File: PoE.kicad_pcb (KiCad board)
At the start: 2 copper layers, 74 parts, among them J101 ARJM11B1-009-AB-EW2, J102 ARJM11B1-009-AB-EW2, Q201 FDC86244, U101 7490220122, U201 TPS23751PWP, U202 TCMT1107, U203 TCMT1107, U204 TLV431ACDBZR

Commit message: Found footprints
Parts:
- added C2002: 22u, footprints:CAP_WCAP-ASLI_06p3X05p5_WRE, F.Cu at (-95.3, -62.0)
- added C2003: 1u, footprints:CAP_WCAP-ASLI_06p3X05p5_WRE, F.Cu at (-95.3, -53.5)
- added C2005: 47u, footprints:CAP_WCAP-ASLI_06p3X05p5_WRE, F.Cu at (83.3, -22.0)
- added C2006: 47u, footprints:CAP_WCAP-ASLI_06p3X05p5_WRE, F.Cu at (-95.3, -45.1)
- added C2007: 47u, footprints:CAP_WCAP-ASLI_06p3X05p5_WRE, F.Cu at (-95.3, -36.6)
- added C2009: 10u, footprints:CAP_WCAP-ASLI_06p3X05p5_WRE, F.Cu at (-95.3, -28.1)
- added C2011: 1u, Capacitor_SMD:C_0402_1005Metric, F.Cu at (-88.8, -54.7)
- added C2012: 10u, Capacitor_SMD:C_0603_1608Metric, F.Cu at (-88.2, -59.4)
- added D1010: LED, LED_SMD:LED_0402_1005Metric, F.Cu at (50.3, -22.5)
- added FB1001: FerriteBead, Resistor_SMD:R_0805_2012Metric, F.Cu at (-54.0, -71.6)
- added FB1002: FerriteBead, Resistor_SMD:R_0805_2012Metric, F.Cu at (-54.0, -68.7)
- added L2001: 4.7u, Inductor_SMD:L_Abracon_ASPI-4030S, F.Cu at (-87.4, -63.5)
- added R1009: 24.9k, Resistor_SMD:R_0402_1005Metric, F.Cu at (-50.3, -72.1)
- added R1010: 2.2k, Resistor_SMD:R_0402_1005Metric, F.Cu at (-50.3, -70.1)
- added R2011: 0.56, Resistor_SMD:R_0603_1608Metric, F.Cu at (-88.2, -56.9)
- added T2001: ~, footprints:750311320, F.Cu at (58.7, -32.5)
- added TP2001: TestPoint, SparkFun-Connector:TestPoint-1.0mm, F.Cu at (-67.5, -30.0)
- added TP2002: TestPoint, SparkFun-Connector:TestPoint-1.0mm, F.Cu at (-67.5, -27.8)
- added U1002: TCMT1107, footprints:SSOP4_4P40X2P85_VIS, F.Cu at (-50.9, -75.4)
- R2001: renamed from R201; footprint SparkFun-Capacitor:C_0402_1005Metric -> Resistor_SMD:R_0402_1005Metric
- R2006: renamed from R206; value 49.9k -> 49.9
- renumbered C101 to C1001, C102 to C1002, C103 to C1003, C104 to C1004, C105 to C1005, C106 to C1006, C107 to C1007, C108 to C1008, C201 to C2001, C204 to C2004, C208 to C2008, C210 to C2010, C213 to C2013, C214 to C2014, CR201 to CR2001, CR202 to CR2002, CR203 to CR2003, D101 to D1001, D102 to D1002, D103 to D1003, D104 to D1004, D109 to D1005, D105 to D1006, D106 to D1007, D107 to D1008, D108 to D1009, D201 to D2001, D202 to D2002, J102 to J1001, J101 to J1002, Q201 to Q2001, R101 to R1001, R102 to R1002, R103 to R1003, R104 to R1004, R105 to R1005, R106 to R1006, R107 to R1007, R108 to R1008, R202 to R2002, R203 to R2003, R204 to R2004, R205 to R2005, R207 to R2007, R208 to R2008, R209 to R2009, R210 to R2010, R212 to R2012, R213 to R2013, R214 to R2014, R215 to R2015, R216 to R2016, R217 to R2017, R218 to R2018, R219 to R2019, R220 to R2020, TP101 to TP1001, TP102 to TP1002, TP103 to TP1003, TP104 to TP1004, TP105 to TP1005, TP106 to TP1006, TP107 to TP1007, U101 to U1001, U201 to U2001, U202 to U2002, U204 to U2003
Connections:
- C1007 pad 1: Net-(D101-K) -> Net-(D1001-K)
- C1007 pad 2: Net-(D105-A) -> Net-(D1006-A)
- CR2001 pad 2: unconnected-(CR201-Pad2) -> Net-(CR2001-Pad2)
- D1001 pad 1: Net-(D101-K) -> Net-(D1001-K)
- D1002 pad 1: Net-(D101-K) -> Net-(D1001-K)
- D1003 pad 1: Net-(D101-K) -> Net-(D1001-K)
- D1004 pad 1: Net-(D101-K) -> Net-(D1001-K)
- D1006 pad 2: Net-(D105-A) -> Net-(D1006-A)
- D1007 pad 2: Net-(D105-A) -> Net-(D1006-A)
- D1008 pad 2: Net-(D105-A) -> Net-(D1006-A)
- D1009 pad 2: Net-(D105-A) -> Net-(D1006-A)
- R2002 pad 2: unconnected-(R202-Pad2) -> Net-(R2002-Pad2)

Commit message: Updating layout
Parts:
- removed E101, E102: MI1206L501R-10, footprints:FB_MI1206L501R-10
- removed R221: 24.9k, Resistor_SMD:R_0402_1005Metric
- removed R222: 10k, Resistor_SMD:R_0402_1005Metric
- removed U203: TCMT1107, footprints:SSOP4_4P40X2P85_VIS
- C1001, C1002, C1003, C1004, C1005, C1006, C1007, C1008, C2001, C2004, C2008, C2010, C2011, C2012, C2013, C2014, D1001, D1002, D1003, D1004, D1006, D1007, D1008, D1009, D1010, D2001, D2002, R1001, R1002, R1003, R1004, R1005, R1006, R1007, R1008, R1009, R1010, R2001, R2002, R2003, R2004, R2005, R2006, R2007, R2008, R2009, R2010, R2012, R2013, R2014, R2015, R2016, R2017, R2018, R2019, R2020, U1002, U2002, U2003: moved to B.Cu
- moved C2012 218.4 mm to (99.0, 53.0)
- moved C2006 216.5 mm to (106.5, 33.5), turned to 90 degrees
- moved C2011 210.9 mm to (93.5, 51.5), turned to 90 degrees
- moved C2007 205.6 mm to (98.0, 33.5), turned to 90 degrees
- moved L2001 200.3 mm to (76.0, 52.5), turned to 180 degrees
- moved C2003 196.0 mm to (74.5, 44.5), turned to -90 degrees
- moved C2002 190.3 mm to (69.0, 34.0), turned to 90 degrees
- moved R2011 188.8 mm to (63.5, 55.5), turned to 180 degrees
- moved TP1001 182.9 mm to (117.5, 25.0)
- moved U1002 182.6 mm to (78.0, 54.0)
- moved R1010 182.2 mm to (83.0, 54.0), turned to 180 degrees
- moved R2015 179.7 mm to (101.0, 52.4), turned to -90 degrees
- moved TP2002 179.4 mm to (104.0, 25.0)
- moved TP1006 178.6 mm to (116.0, 25.0)
- moved R2019 178.3 mm to (101.0, 54.5), turned to -90 degrees
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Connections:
- D1006 pad 1: unconnected-(D1006-K-Pad1) -> /A_IN
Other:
- board outline added: 102.5 x 33.5 mm
- copper layers 2 -> 4

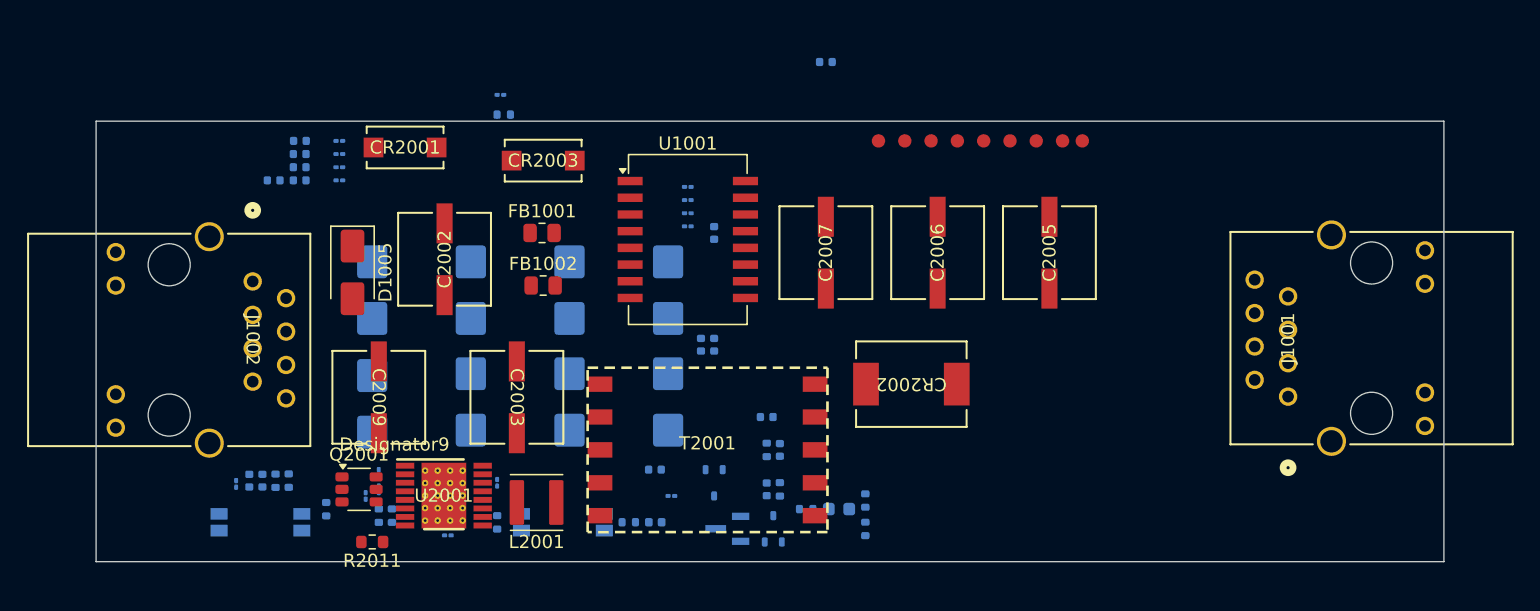
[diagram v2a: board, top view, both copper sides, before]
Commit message: Changed all passive footprints to 0805
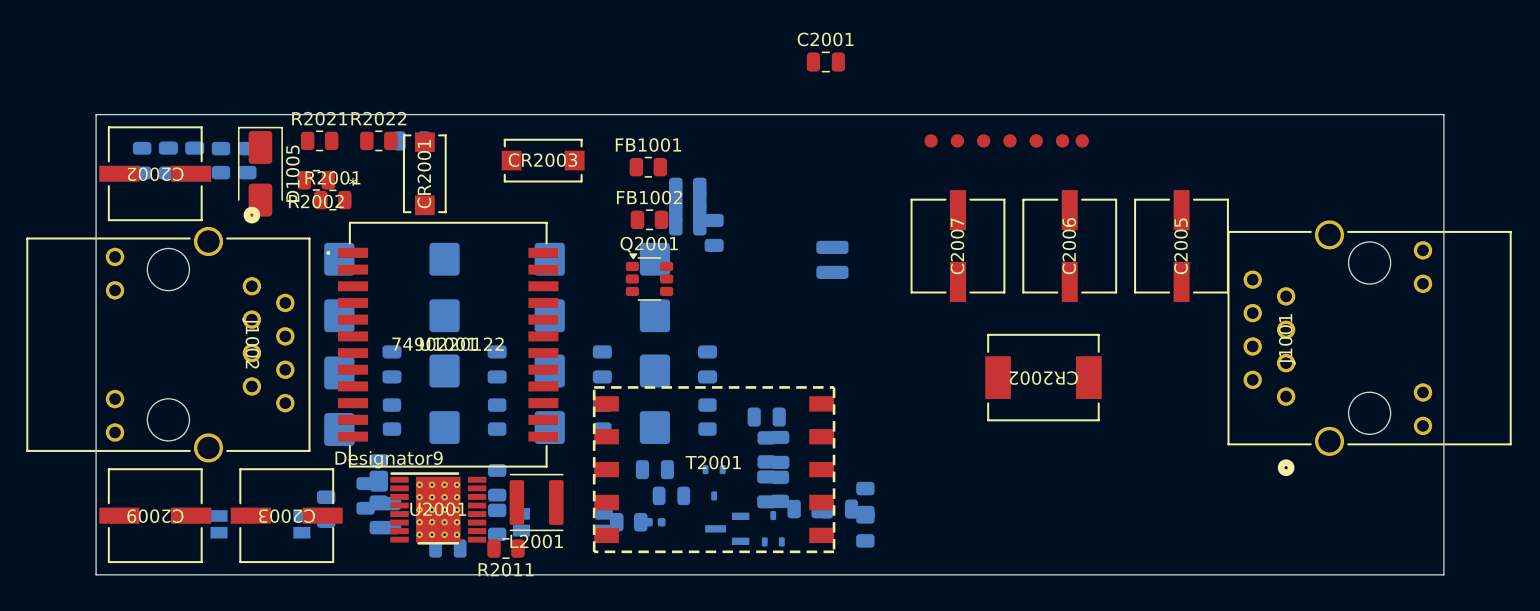
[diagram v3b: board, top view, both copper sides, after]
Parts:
- removed TP2001, TP2002: TestPoint, SparkFun-Connector:TestPoint-1.0mm
- added R2021: 0, Resistor_SMD:R_0805_2012Metric, F.Cu at (59.5, 25.0)
- added R2022: 0, Resistor_SMD:R_0805_2012Metric, F.Cu at (64.0, 25.0)
- C1001, C1002, C1003, C1004, C1005, C1006, C1007, C1008, C2004, C2008, C2010, C2013, C2014: footprint SparkFun-Capacitor:C_0402_1005Metric -> Capacitor_SMD:C_0805_2012Metric
- C2001: footprint SparkFun-Capacitor:C_0402_1005Metric -> Capacitor_SMD:C_0805_2012Metric; moved to F.Cu
- C2011: footprint Capacitor_SMD:C_0402_1005Metric -> Capacitor_SMD:C_0805_2012Metric
- C2012: footprint Capacitor_SMD:C_0603_1608Metric -> Capacitor_SMD:C_0805_2012Metric
- R1001, R1002, R1003, R1004, R1005, R1006, R1007, R1008: footprint Resistor_SMD:R_01005_0402Metric -> Resistor_SMD:R_0805_2012Metric
- R1009, R1010, R2003, R2012, R2013, R2014, R2015, R2016, R2017, R2018, R2019, R2020: footprint Resistor_SMD:R_0402_1005Metric -> Resistor_SMD:R_0805_2012Metric
- R2001: footprint Resistor_SMD:R_0402_1005Metric -> Resistor_SMD:R_0805_2012Metric; moved to F.Cu
- R2002: footprint Resistor_SMD:R_01005_0402Metric -> Resistor_SMD:R_0805_2012Metric; moved to F.Cu
- R2004, R2005, R2006, R2007, R2008, R2009, R2010: footprint Resistor_SMD:R_01005_0402Metric -> LED_SMD:LED_0805_2012Metric
- R2011: footprint Resistor_SMD:R_0603_1608Metric -> Resistor_SMD:R_0805_2012Metric
- U1001: footprint Transformer_SMD:Transformer_Ethernet_Wuerth_749013011A -> footprints:7490220122
- moved C1005 34.0 mm to (89.0, 42.0), turned to -90 degrees
- moved R1008 33.3 mm to (89.0, 46.0), turned to 90 degrees
- moved R1007 27.6 mm to (81.0, 46.0), turned to -90 degrees
- moved C1004 27.5 mm to (81.0, 42.0), turned to -90 degrees
- moved Q2001 27.3 mm to (84.6, 35.5)
- moved R2008 25.6 mm to (46.0, 26.5)
- moved U1001 25.5 mm to (62.0, 33.5)
- moved C2013 25.1 mm to (48.0, 26.5)
- moved C2014 24.9 mm to (50.0, 26.5)
- moved R2017 24.7 mm to (52.0, 26.5)
- moved R2018 24.5 mm to (54.0, 26.5)
- moved R1006 23.3 mm to (73.0, 46.0), turned to -90 degrees
- moved C2002 22.9 mm to (47.0, 27.5), turned to 180 degrees
- moved C1003 21.9 mm to (73.0, 42.0), turned to -90 degrees
- moved R1005 21.4 mm to (65.0, 46.0), turned to -90 degrees
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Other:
- board size 102.5 x 33.5 mm -> 102.5 x 35 mm

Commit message: Starting Layout
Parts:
- D1005, FB1001, FB1002: moved to B.Cu
- J1001, J1002: value ARJM11B1-009-AB-EW2 -> 8P8C_LED_Shielded_x2
- moved R2001 73.0 mm to (130.1, 56.0)
- moved R2003 73.0 mm to (125.6, 56.0)
- moved U2002 56.5 mm to (104.0, 26.0)
- moved R2002 52.4 mm to (109.8, 47.5)
- moved R2004 52.4 mm to (108.5, 46.0)
- moved D1005 44.8 mm to (98.0, 40.0)
- moved U1002 35.7 mm to (104.0, 29.5)
- moved U1001 31.1 mm to (92.5, 39.6), turned to 180 degrees
- moved C2003 28.9 mm to (71.5, 28.5), turned to 90 degrees
- moved Q2001 23.0 mm to (71.0, 54.0)
- moved FB1001 20.2 mm to (101.5, 38.0), turned to 180 degrees
- moved FB1002 20.2 mm to (101.6, 42.0), turned to 180 degrees
- moved CR2003 19.4 mm to (72.5, 45.5), turned to 90 degrees
- moved L2001 19.0 mm to (67.5, 35.5), turned to 0 degrees
- moved C2002 16.5 mm to (63.5, 28.5), turned to 90 degrees
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- renumbered R2022 to R2001, R2001 to R2002, R2021 to R2003, R2002 to R2004, R2003 to R2005, R2004 to R2006, R2005 to R2007, R2006 to R2008, R2007 to R2009, R2008 to R2010, R2009 to R2011, R2010 to R2012, R2011 to R2013, R2012 to R2014, R2013 to R2015, R2014 to R2016, R2015 to R2017, R2016 to R2018, R2017 to R2019, R2018 to R2020, R2019 to R2021, R2020 to R2022
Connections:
- J1001 pad 10: (no net) -> unconnected-(J1001-Pad10)
- J1001 pad 11: (no net) -> unconnected-(J1001-Pad11)
- J1001 pad 12: (no net) -> unconnected-(J1001-Pad12)
- J1002 pad 10: (no net) -> unconnected-(J1002-Pad10)
- J1002 pad 11: (no net) -> unconnected-(J1002-Pad11)
- J1002 pad 12: (no net) -> unconnected-(J1002-Pad12)
- U2001 pad 6: /Flyback/T2P -> T2P
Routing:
- added copper zone on B.Cu, net GND
- added copper zone on F.Cu, net GND
- added copper zone on F.Cu, net GNDPWR

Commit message: Still needs a lot of work
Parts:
- moved R2001 77.0 mm to (58.6, 27.4)
- moved R2003 77.0 mm to (54.1, 27.4)
- moved R2004 56.6 mm to (54.1, 30.4)
- moved R2002 53.9 mm to (58.6, 30.4)
- moved C2001 51.8 mm to (140.3, 48.9), turned to 90 degrees
- moved TP1004 41.5 mm to (140.8, 41.4), turned to 90 degrees
- moved C2007 38.8 mm to (130.5, 49.7), turned to 180 degrees
- moved TP1007 38.8 mm to (140.8, 39.4), turned to 90 degrees
- moved TP1003 36.1 mm to (140.8, 37.4), turned to 90 degrees
- moved TP1002 33.3 mm to (140.8, 35.4), turned to 90 degrees
- moved C1008 31.5 mm to (67.0, 56.5)
- moved TP1005 30.6 mm to (140.8, 33.4), turned to 90 degrees
- moved TP1006 28.0 mm to (140.8, 31.4), turned to 90 degrees
- moved J1001 27.7 mm to (114.5, 28.6), turned to 180 degrees
- moved C2006 27.2 mm to (130.5, 41.2), turned to 180 degrees
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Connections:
- net /POE0 renamed /POE0_P
- net /POE1 renamed /POE0_N
- net /POE2 renamed /POE1_P
- net /POE3 renamed /POE1_N
- net /POE4 renamed /POE2_P
- net /POE5 renamed /POE2_N
- net /POE6 renamed /POE3_P
- net /POE7 renamed /POE3_N
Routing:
- net /POE1_N: track 0.00 -> 31.5 mm
- net /POE3_N: track 0.00 -> 25.3 mm
- net /POE0_N: track 0.00 -> 22.3 mm
- net /POE3_P: track 0.00 -> 22.0 mm
- net /POE2_N: track 0.00 -> 18.4 mm
- net /POE2_P: track 0.00 -> 16.3 mm
- net Net-(CR2003-Pad2): track 0.00 -> 14.9 mm
- net /POE1_P: track 0.00 -> 13.1 mm
- net /POE0_P: track 0.00 -> 11.5 mm
- net /D_IN: track 0.00 -> 6.02 mm, vias 0 -> 4
- net Net-(Q2001-S): track 0.00 -> 5.79 mm
- net /Flyback/VC: track 0.00 -> 1.27 mm
- net GND: vias 0 -> 6
- net /C_IN: vias 0 -> 4
- added copper zone on F.Cu, net /C_IN
- added copper zone on In1.Cu, net /C_IN
- added copper zone on F.Cu, net /D_IN
- added copper zone on In1.Cu, net /D_IN
- added copper zone on In1.Cu, net GND
- added copper zone on In2.Cu, net GND
- removed copper zone on F.Cu, net GNDPWR

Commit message: Updating layout
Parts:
- moved C1005 31.9 mm to (90.0, 73.5)
- moved R1008 31.9 mm to (90.0, 77.5)
- moved C1004 24.2 mm to (82.0, 73.5)
- moved R1007 24.2 mm to (82.0, 77.5)
- moved C1002 24.0 mm to (66.5, 73.5)
- moved C1003 24.0 mm to (74.5, 73.5)
- moved C1008 24.0 mm to (66.5, 80.5)
- moved R1005 24.0 mm to (66.5, 77.5)
- moved R1006 24.0 mm to (74.5, 77.5)
- moved C2008 23.3 mm to (75.8, 44.5), turned to 90 degrees
- moved R2011 23.3 mm to (78.5, 50.5), turned to -90 degrees
- moved R2005 23.2 mm to (76.8, 55.0)
- moved C2004 22.2 mm to (78.8, 55.0)
- moved D1006 20.9 mm to (62.5, 73.2)
- moved D1001 20.9 mm to (62.5, 64.5)
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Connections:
- net Net-(C2003-Pad1) renamed /Flyback/T_PRI
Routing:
- net GND: track 0.00 -> 1.27 mm, vias 6 -> 4
- net /Flyback/VC: track 1.27 -> 0.00 mm
- net /Flyback/T_PRI: vias 0 -> 1
- net /D_IN: vias 4 -> 5
- net /C_IN: vias 4 -> 5
- net /B_IN: vias 0 -> 6
- net /A_IN: vias 0 -> 6
- added copper zone on B.Cu, net VSS
- added copper zone on F.Cu, net VSS
- added copper zone on In1.Cu, net VSS
- added copper zone on In2.Cu, net VSS
- removed copper zone on F.Cu, net /C_IN
- removed copper zone on In1.Cu, net /C_IN
- removed copper zone on B.Cu, net GND
- removed copper zone on F.Cu, net GND
- removed copper zone on In1.Cu, net GND
- removed copper zone on In2.Cu, net GND

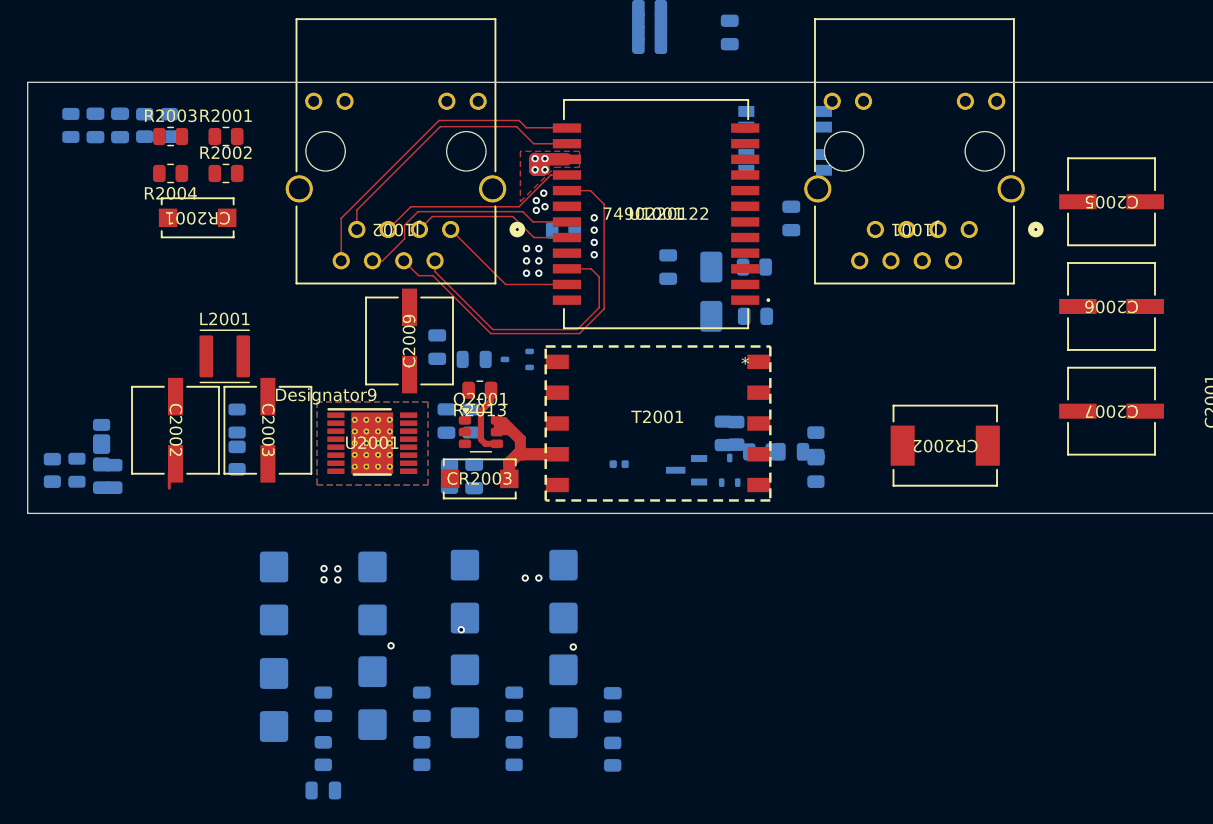
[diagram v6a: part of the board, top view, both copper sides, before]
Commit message: Added power planes
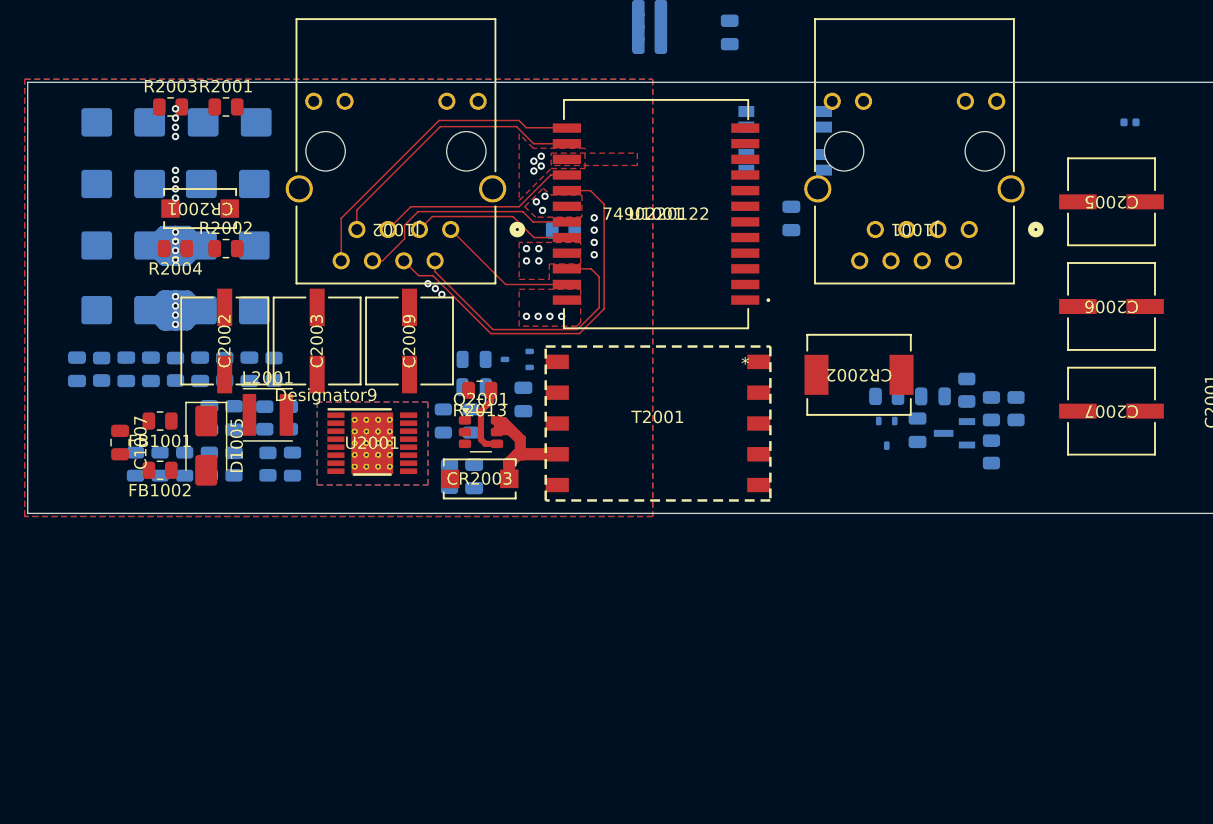
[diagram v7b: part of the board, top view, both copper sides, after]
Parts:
- C1007, D1005, FB1001, FB1002: moved to F.Cu
- moved R2022 78.4 mm to (122.8, 49.5)
- moved FB1002 49.9 mm to (53.2, 54.5)
- moved D1010 49.9 mm to (132.0, 26.2)
- moved FB1001 49.8 mm to (53.2, 50.5)
- moved D1006 48.5 mm to (50.2, 26.2), turned to 180 degrees
- moved D1009 47.5 mm to (50.2, 41.5), turned to 180 degrees
- moved C1007 46.7 mm to (50.0, 52.2)
- moved D1007 46.4 mm to (50.2, 31.2), turned to 180 degrees
- moved D1008 45.9 mm to (50.2, 36.2), turned to 180 degrees
- moved D1005 42.9 mm to (57.0, 52.5)
- moved R1008 41.6 mm to (62.5, 46.3)
- moved C1005 40.2 mm to (60.5, 46.3)
- moved C1008 39.6 mm to (46.5, 46.3), turned to -90 degrees
- moved R1007 39.1 mm to (58.5, 46.3), turned to 90 degrees
- moved R2010 38.6 mm to (76.2, 50.5), turned to 90 degrees
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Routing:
- net /C_IN: track 0.00 -> 21.4 mm, vias 5 -> 7
- net /D_IN: track 6.02 -> 21.8 mm, vias 5 -> 8
- net GND: track 1.27 -> 0.00 mm
- net /Flyback/T_PRI: vias 1 -> 0
- net /B_IN: vias 6 -> 11
- net /A_IN: vias 6 -> 8
- added copper zone on F.Cu, net /A_IN
- added copper zone on In2.Cu, net /A_IN
- added copper zone on F.Cu, net /B_IN
- added copper zone on In1.Cu, net /B_IN
- added copper zone on In2.Cu, net /B_IN
- added copper zone on F.Cu, net /C_IN
- added copper zone on In2.Cu, net /C_IN
- added copper zone on B.Cu, net GND
- added copper zone on F.Cu, net GND
- added copper zone on In1.Cu, net GND
- added copper zone on In2.Cu, net GND

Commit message: Added routing
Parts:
- C2002: value 22u -> 47u
- C2003: footprint footprints:CAP_WCAP-ASLI_06p3X05p5_WRE -> Capacitor_SMD:C_0805_2012Metric
- moved R2002 15.6 mm to (58.6, 20.9)
- moved R2004 15.5 mm to (54.5, 21.0)
- moved CR2001 15.0 mm to (48.5, 20.6)
- moved C2003 11.3 mm to (61.2, 54.2), turned to 180 degrees
- moved C2002 7.50 mm to (66.0, 44.0)
- moved R2003 6.31 mm to (54.5, 18.7)
- moved R2001 6.30 mm to (58.4, 18.7)
- moved R1007 4.10 mm to (62.6, 46.3)
- moved C1004 4.00 mm to (60.5, 46.3)
- moved C1005 4.00 mm to (56.5, 46.3)
- moved R1008 4.00 mm to (58.5, 46.3)
- moved L2001 0.54 mm to (61.5, 50.2)
- moved FB1002 0.50 mm to (53.2, 54.0)
- moved D1001 0.15 mm to (58.8, 26.2)
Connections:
- net Net-(D1001-K) renamed /VDD_PRIME
- net Net-(D1006-A) renamed /VSS_PRIME
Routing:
- net /A_IN: track 0.00 -> 41.4 mm
- net /B_IN: track 0.00 -> 35.5 mm
- net Net-(U2001-CLS): track 0.00 -> 18.3 mm, vias 0 -> 2
- net Net-(C1008-Pad1): track 0.00 -> 18.1 mm
- net /VSS_PRIME: track 0.00 -> 17.9 mm, vias 0 -> 8
- net /VDD_PRIME: track 0.00 -> 17.9 mm
- net Net-(U2001-DEN): track 0.00 -> 17.1 mm, vias 0 -> 2
- net Net-(U2001-VB): track 0.00 -> 12.8 mm
- net /C_IN: track 21.4 -> 32.4 mm
- net Net-(U2001-RT): track 0.00 -> 9.52 mm, vias 0 -> 2
- net Net-(U2001-CTL): track 0.00 -> 5.27 mm
- net /D_IN: track 21.8 -> 26.1 mm
- net VDD: track 0.00 -> 3.23 mm, vias 0 -> 1
- net Net-(C2013-Pad1): track 0.00 -> 2.52 mm
- net Net-(C1004-Pad2): track 0.00 -> 2.12 mm
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- added copper zone on F.Cu, net /VDD_PRIME
- added copper zone on B.Cu, net /VSS_PRIME
- added copper zone on F.Cu, net /VSS_PRIME
